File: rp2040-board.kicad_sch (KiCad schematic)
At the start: 100 parts, among them J1 24V IN, J10 E0-RUNOUT, J11 FAN1, J12 FAN2, J13 FAN3, J14 HB, J15 E0, J16 TH-E0, J2 USB4105-GF-A, J3 PGA2040, J4 3_GPIO, J5 PROBE, J6 X-ENDSTOP, J7 TH-HB, J8 Y-ENDSTOP, J9 Z-ENDSTOP, Q1 AO3400C, Q2 AO3400C, Q3 AO3400C, SW1 SW_MEC_5E, U1 LD1086DT33TR, U2 TPS5450DDAR, U3 74HCT365D,653, U4 FDS8896, U5 FDS8896

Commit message: almost done with layout...
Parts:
- removed D10, D11, D3, D7, D8, D9: Red LED, Diode_SMD:D_1210_3225Metric_Pad1.42x2.65mm_HandSolder, symbol Device:LED
- removed R3: 1K, Resistor_SMD:R_1206_3216Metric_Pad1.30x1.75mm_HandSolder, symbol Device:R_Small
- removed R35, R36, R37, R38, R39: 10K, Resistor_SMD:R_1206_3216Metric_Pad1.30x1.75mm_HandSolder, symbol Device:R_Small
- removed U1: LD1086DT33TR, LD1086DT33TR:VREG_L78M08CDT-TR, symbol LD1086DT33TR:LD1086DT33TR
- added U1: AMS1117-3.3, SOT229P700X180-4N, symbol AMS1117-3.3:AMS1117-3.3
- C1, C10, C2, C3: footprint Capacitor_SMD:C_1206_3216Metric_Pad1.33x1.80mm_HandSolder -> Capacitor_SMD:C_0805_2012Metric_Pad1.18x1.45mm_HandSolder
- C12, C13, C14, C15, C16, C17, C18, C4, C5, C8, C9: footprint Capacitor_SMD:C_1206_3216Metric_Pad1.33x1.80mm_HandSolder -> Capacitor_SMD:C_0805_2012Metric_Pad1.18x1.45mm_HandSolder; MANUFACTURER Murata -> Samsung Electro Mechanics
- C6: renamed from C7; footprint Capacitor_SMD:C_1210_3225Metric_Pad1.33x2.70mm_HandSolder -> Capacitor_SMD:C_0805_2012Metric_Pad1.18x1.45mm_HandSolder; MANUFACTURER Taiyo Yuden -> Murata
- C7: renamed from C6; footprint Capacitor_SMD:C_1206_3216Metric_Pad1.33x1.80mm_HandSolder -> Capacitor_SMD:C_0805_2012Metric_Pad1.18x1.45mm_HandSolder; MANUFACTURER Murata -> Samsung Electro Mechanics
- D1: footprint Diode_SMD:D_SMC_Handsoldering -> Diode_SMD:D_SMA_Handsoldering; MANUFACTURER onsemi -> MDD
- D2: footprint Diode_SMD:D_SMB-SMC_Universal_Handsoldering -> Diode_SMD:D_SMB_Handsoldering
- D3: renamed from D4; footprint Diode_SMD:D_SMC_Handsoldering -> Diode_SMD:D_SMA_Handsoldering
- F2: footprint 01000063Z:01000063Z -> 01000063Z; symbol Device:Fuse -> 01000063Z:01000063Z
- R1: footprint Resistor_SMD:R_1206_3216Metric_Pad1.30x1.75mm_HandSolder -> Resistor_SMD:R_0805_2012Metric_Pad1.20x1.40mm_HandSolder; MANUFACTURER Panasonic -> YAGEO
- R10: renamed from R11; footprint Resistor_SMD:R_1206_3216Metric_Pad1.30x1.75mm_HandSolder -> Resistor_SMD:R_0805_2012Metric_Pad1.20x1.40mm_HandSolder; MANUFACTURER Vishay Intertech -> YAGEO
- R11: renamed from R12; footprint Resistor_SMD:R_1206_3216Metric_Pad1.30x1.75mm_HandSolder -> Resistor_SMD:R_0805_2012Metric_Pad1.20x1.40mm_HandSolder; MANUFACTURER Vishay Intertech -> YAGEO
- R12: renamed from R13; footprint Resistor_SMD:R_1210_3225Metric_Pad1.30x2.65mm_HandSolder -> Resistor_SMD:R_0805_2012Metric_Pad1.20x1.40mm_HandSolder
- R13: renamed from R14; footprint Resistor_SMD:R_1210_3225Metric_Pad1.30x2.65mm_HandSolder -> Resistor_SMD:R_0805_2012Metric_Pad1.20x1.40mm_HandSolder
- R14: renamed from R15; footprint Resistor_SMD:R_1206_3216Metric_Pad1.30x1.75mm_HandSolder -> Resistor_SMD:R_0805_2012Metric_Pad1.20x1.40mm_HandSolder; MANUFACTURER Vishay Intertech -> YAGEO
- R15: renamed from R16; footprint Resistor_SMD:R_1206_3216Metric_Pad1.30x1.75mm_HandSolder -> Resistor_SMD:R_0805_2012Metric_Pad1.20x1.40mm_HandSolder; MANUFACTURER Vishay Intertech -> YAGEO
- R16: renamed from R17; footprint Resistor_SMD:R_1206_3216Metric_Pad1.30x1.75mm_HandSolder -> Resistor_SMD:R_0805_2012Metric_Pad1.20x1.40mm_HandSolder
- R17: renamed from R18; footprint Resistor_SMD:R_1206_3216Metric_Pad1.30x1.75mm_HandSolder -> Resistor_SMD:R_0805_2012Metric_Pad1.20x1.40mm_HandSolder; MANUFACTURER Panasonic -> YAGEO
- R18: renamed from R19; footprint Resistor_SMD:R_1206_3216Metric_Pad1.30x1.75mm_HandSolder -> Resistor_SMD:R_0805_2012Metric_Pad1.20x1.40mm_HandSolder
- R19: renamed from R20; footprint Resistor_SMD:R_1206_3216Metric_Pad1.30x1.75mm_HandSolder -> Resistor_SMD:R_0805_2012Metric_Pad1.20x1.40mm_HandSolder; MANUFACTURER Panasonic -> YAGEO
- R2: footprint Resistor_SMD:R_1206_3216Metric_Pad1.30x1.75mm_HandSolder -> Resistor_SMD:R_0805_2012Metric_Pad1.20x1.40mm_HandSolder; MANUFACTURER Vishay Intertech -> YAGEO
- R20: renamed from R21; footprint Resistor_SMD:R_1206_3216Metric_Pad1.30x1.75mm_HandSolder -> Resistor_SMD:R_0805_2012Metric_Pad1.20x1.40mm_HandSolder; MANUFACTURER Vishay Intertech -> YAGEO
- R21: renamed from R22; footprint Resistor_SMD:R_1206_3216Metric_Pad1.30x1.75mm_HandSolder -> Resistor_SMD:R_0805_2012Metric_Pad1.20x1.40mm_HandSolder; MANUFACTURER Vishay Intertech -> YAGEO
- R22: renamed from R23; footprint Resistor_SMD:R_1206_3216Metric_Pad1.30x1.75mm_HandSolder -> Resistor_SMD:R_0805_2012Metric_Pad1.20x1.40mm_HandSolder; MANUFACTURER Vishay Intertech -> YAGEO
- R23: renamed from R24; footprint Resistor_SMD:R_1206_3216Metric_Pad1.30x1.75mm_HandSolder -> Resistor_SMD:R_0805_2012Metric_Pad1.20x1.40mm_HandSolder; MANUFACTURER Vishay Intertech -> YAGEO
- R24: renamed from R25; footprint Resistor_SMD:R_1206_3216Metric_Pad1.30x1.75mm_HandSolder -> Resistor_SMD:R_0805_2012Metric_Pad1.20x1.40mm_HandSolder; MANUFACTURER Vishay Intertech -> YAGEO
- R25: renamed from R26; footprint Resistor_SMD:R_1210_3225Metric_Pad1.30x2.65mm_HandSolder -> Resistor_SMD:R_0805_2012Metric_Pad1.20x1.40mm_HandSolder
- R26: renamed from R27; footprint Resistor_SMD:R_1206_3216Metric_Pad1.30x1.75mm_HandSolder -> Resistor_SMD:R_0805_2012Metric_Pad1.20x1.40mm_HandSolder
- R27: renamed from R28; footprint Resistor_SMD:R_1206_3216Metric_Pad1.30x1.75mm_HandSolder -> Resistor_SMD:R_0805_2012Metric_Pad1.20x1.40mm_HandSolder; MANUFACTURER Panasonic -> YAGEO
- R28: renamed from R29; footprint Resistor_SMD:R_1206_3216Metric_Pad1.30x1.75mm_HandSolder -> Resistor_SMD:R_0805_2012Metric_Pad1.20x1.40mm_HandSolder
- R29: renamed from R30; footprint Resistor_SMD:R_1206_3216Metric_Pad1.30x1.75mm_HandSolder -> Resistor_SMD:R_0805_2012Metric_Pad1.20x1.40mm_HandSolder; MANUFACTURER Panasonic -> YAGEO
- R3: renamed from R4; footprint Resistor_SMD:R_1206_3216Metric_Pad1.30x1.75mm_HandSolder -> Resistor_SMD:R_0805_2012Metric_Pad1.20x1.40mm_HandSolder; MANUFACTURER Vishay Intertech -> YAGEO
- R30: renamed from R31; footprint Resistor_SMD:R_1206_3216Metric_Pad1.30x1.75mm_HandSolder -> Resistor_SMD:R_0805_2012Metric_Pad1.20x1.40mm_HandSolder
- R31: renamed from R32; footprint Resistor_SMD:R_1206_3216Metric_Pad1.30x1.75mm_HandSolder -> Resistor_SMD:R_0805_2012Metric_Pad1.20x1.40mm_HandSolder; MANUFACTURER Panasonic -> YAGEO
- R32: renamed from R33; footprint Resistor_SMD:R_1210_3225Metric_Pad1.30x2.65mm_HandSolder -> Resistor_SMD:R_0805_2012Metric_Pad1.20x1.40mm_HandSolder
- R33: renamed from R34; footprint Resistor_SMD:R_1206_3216Metric_Pad1.30x1.75mm_HandSolder -> Resistor_SMD:R_0805_2012Metric_Pad1.20x1.40mm_HandSolder; MANUFACTURER Vishay Intertech -> YAGEO
- R4: renamed from R5; footprint Resistor_SMD:R_1206_3216Metric_Pad1.30x1.75mm_HandSolder -> Resistor_SMD:R_0805_2012Metric_Pad1.20x1.40mm_HandSolder; MANUFACTURER Vishay Intertech -> YAGEO
- R5: renamed from R6; footprint Resistor_SMD:R_1210_3225Metric_Pad1.30x2.65mm_HandSolder -> Resistor_SMD:R_0805_2012Metric_Pad1.20x1.40mm_HandSolder
- R6: renamed from R7; footprint Resistor_SMD:R_1206_3216Metric_Pad1.30x1.75mm_HandSolder -> Resistor_SMD:R_0805_2012Metric_Pad1.20x1.40mm_HandSolder; MANUFACTURER Vishay Intertech -> YAGEO
- R7: renamed from R8; footprint Resistor_SMD:R_1206_3216Metric_Pad1.30x1.75mm_HandSolder -> Resistor_SMD:R_0805_2012Metric_Pad1.20x1.40mm_HandSolder; MANUFACTURER Vishay Intertech -> YAGEO
- R8: renamed from R9; footprint Resistor_SMD:R_1206_3216Metric_Pad1.30x1.75mm_HandSolder -> Resistor_SMD:R_0805_2012Metric_Pad1.20x1.40mm_HandSolder; MANUFACTURER Vishay Intertech -> YAGEO
- R9: renamed from R10; footprint Resistor_SMD:R_1206_3216Metric_Pad1.30x1.75mm_HandSolder -> Resistor_SMD:R_0805_2012Metric_Pad1.20x1.40mm_HandSolder; MANUFACTURER Vishay Intertech -> YAGEO
- RN1, RN2, RN3, RN4: footprint Resistor_SMD:R_Array_Convex_4x1206 -> Resistor_SMD:R_Array_Convex_4x0603; MANUFACTURER Bourns -> CTS Electronic Components
- SW1: footprint Button_Switch_SMD:SW_Push_1P1T_NO_CK_KSC6xxJ -> 1825966-1:SW_1825966-1
- renumbered D5 to D4, D6 to D5
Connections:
- net +3.3V: now also U1.2 (VOUT)
- net +5V: now also C14.1, U3.16 (VCC)
- net GND: now also U1.1 (ADJ/GND)
- net VCC: now also F2.1
- net at J1.1 (Pin_1): now also F2.3, F2.4; no longer D2.1 (A)
- net at J1.2 (Pin_2): now also D2.1 (A); no longer F2.1
- net at F1.2: now also U1.3 (VIN)
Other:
- moved on the sheet: C1, C10, C11, C12, C15, C2, C3, C5, C6, C7, C8, D1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

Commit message: I am in immense pain
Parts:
- removed SW1: SW_MEC_5E, 1825966-1:SW_1825966-1, symbol Switch:SW_MEC_5E
- added JP1: RUN, Connector_PinHeader_2.54mm:PinHeader_1x02_P2.54mm_Vertical, symbol Jumper:Jumper_2_Open
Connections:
- net GND: now also JP1.1 (A)
- net HEATERS: no longer R26.2, R27.2, U3.3 (1Y)
- net VCC: now also F2.3, F2.4, J14.1 (Pin_1), J15.1 (Pin_1); no longer F2.1, F2.2, J14.2 (Pin_2), J15.2 (Pin_2)
- net at U4.5 (DRAIN-3), U4.6 (DRAIN-2), U4.7 (DRAIN-1)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: now also J14.2 (Pin_2); no longer J14.1 (Pin_1)
- net at U5.5 (DRAIN-3), U5.6 (DRAIN-2), U5.7 (DRAIN-1)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: now also J15.2 (Pin_2); no longer J15.1 (Pin_1)
- net at C5.2, J3.A4 (RUN), R2.2: now also JP1.2 (B)
- new net: R26.2, R27.2, U3.3 (1Y)
- new net: F2.1, F2.2, J1.1 (Pin_1)
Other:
- moved on the sheet: F2, J14, J15

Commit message: finished, for now, finally
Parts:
- removed J4: 3_GPIO, Connector_PinSocket_2.54mm:PinSocket_1x03_P2.54mm_Vertical, symbol Connector:Conn_01x03_Female
- added J22: Exp. Header 2, Connector_PinHeader_2.54mm:PinHeader_1x02_P2.54mm_Vertical, symbol Connector:Conn_01x02_Male
- added J23: Exp. Header 3, Connector_PinHeader_2.54mm:PinHeader_1x02_P2.54mm_Vertical, symbol Connector:Conn_01x02_Male
- added J4: Exp. Header 1, symbol Connector:Conn_01x02_Male
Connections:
- net +3.3V: now also J22.1 (Pin_1)
- net +5V: now also J23.1 (Pin_1)
- net E0DIR: now also J3.G4 (GPIO14); no longer J3.G3 (GPIO12), RN4.1 (R1.1)
- net E0EN: now also J3.G3 (GPIO12); no longer J3.G4 (GPIO14), RN4.3 (R3.1)
- net E0STP: no longer RN4.2 (R2.1)
- net GND: now also J23.2 (Pin_2)
- net XDIR: now also J3.C2 (GPIO2); no longer J3.B1 (GPIO0), RN1.1 (R1.1)
- net XEN: now also J3.B1 (GPIO0); no longer J3.C2 (GPIO2), RN1.3 (R3.1)
- net XSTP: no longer RN1.2 (R2.1)
- net YDIR: now also J3.E2 (GPIO6); no longer J3.D2 (GPIO4), RN2.1 (R1.1)
- net YEN: now also J3.D2 (GPIO4); no longer J3.E2 (GPIO6), RN2.3 (R3.1)
- net YSTP: no longer RN2.2 (R2.1)
- net ZDIR: now also J3.H2 (GPIO10); no longer J3.F2 (GPIO8), RN3.1 (R1.1)
- net ZEN: now also J3.F2 (GPIO8); no longer J3.H2 (GPIO10), RN3.3 (R3.1)
- net ZSTP: no longer RN3.2 (R2.1)
- net GPIO22: now reaches J3.F7 (GPIO22)
- net GPIO22: now also J22.2 (Pin_2)
- net GPIO21: now reaches J3.F8 (GPIO21)
- net GPIO21: now also J4.2 (Pin_2)
- net GPIO20: now reaches J3.G8 (GPIO20)
- net GPIO20: now also J4.1 (Pin_1)
- new net E0DIRR: RN4.1 (R1.1)
- new net E0ENR: RN4.3 (R3.1)
- new net E0STPR: RN4.2 (R2.1)
- new net XDIRR: RN1.1 (R1.1)
- new net XENR: RN1.3 (R3.1)
- new net XSTPR: RN1.2 (R2.1)
- new net YDIRR: RN2.1 (R1.1)
- new net YENR: RN2.3 (R3.1)
- new net YSTPR: RN2.2 (R2.1)
- new net ZDIRR: RN3.1 (R1.1)
- new net ZENR: RN3.3 (R3.1)
- new net ZSTPR: RN3.2 (R2.1)
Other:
- moved on the sheet: RN1, RN2, RN3, RN4

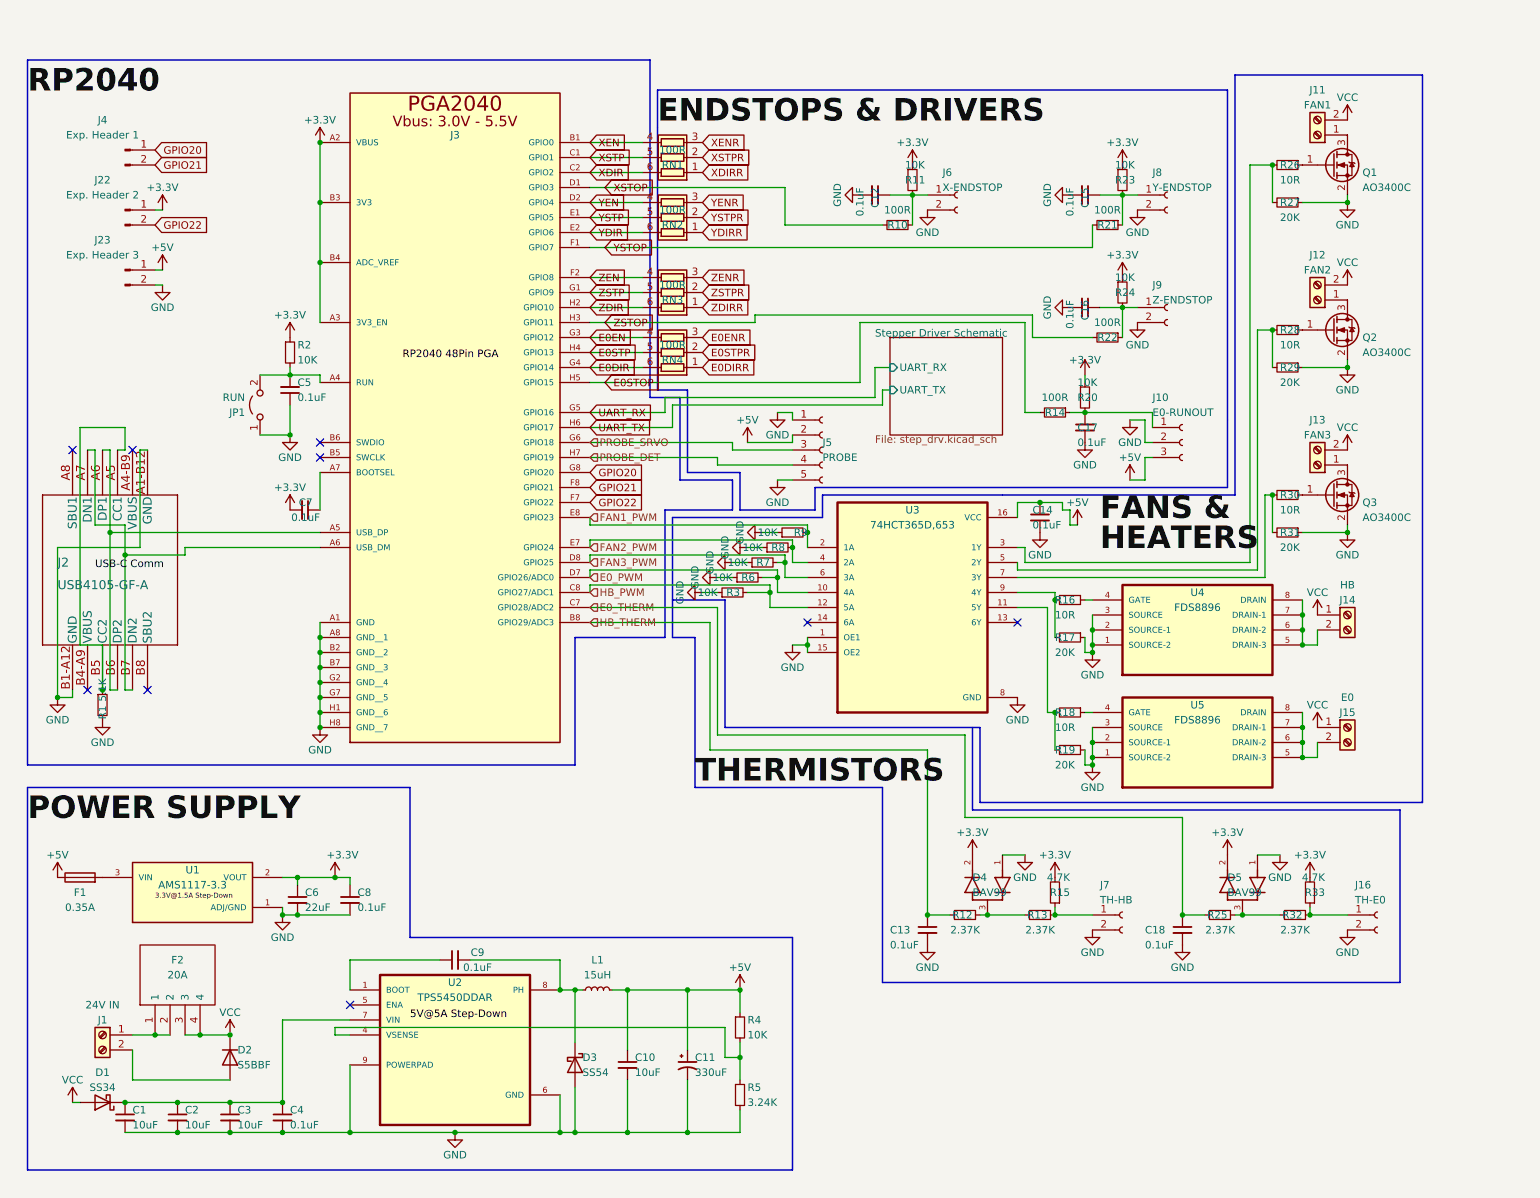
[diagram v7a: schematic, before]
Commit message: Rev 1.1 - PT1000 + ADC/I2C GPIO
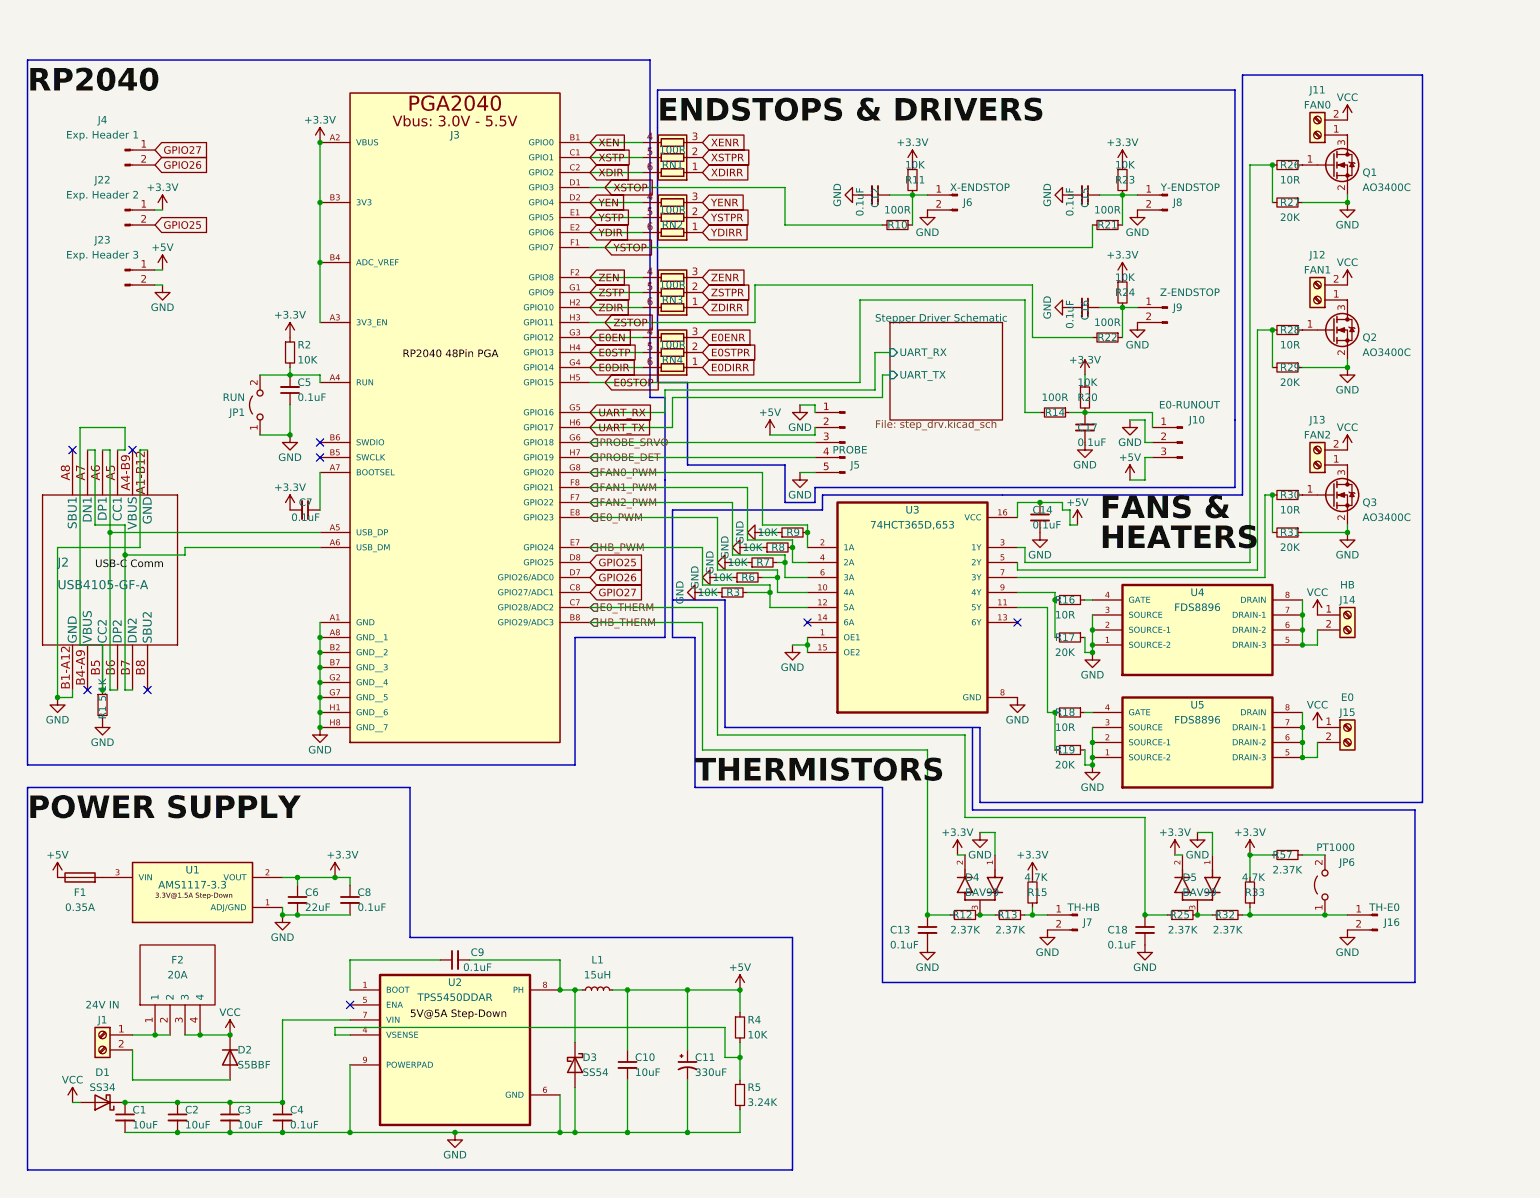
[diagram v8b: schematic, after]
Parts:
- added JP6: PT1000, Connector_PinHeader_2.54mm:PinHeader_1x02_P2.54mm_Vertical, symbol Jumper:Jumper_2_Open
- added R57: 2.37K, Resistor_SMD:R_0805_2012Metric_Pad1.20x1.40mm_HandSolder, symbol Device:R_Small
- J10: symbol Connector:Conn_01x03_Female -> Connector:Conn_01x03_Male
- J11: value FAN1 -> FAN0
- J12: value FAN2 -> FAN1
- J13: value FAN3 -> FAN2
- J16, J6, J7, J8, J9: symbol Connector:Conn_01x02_Female -> Connector:Conn_01x02_Male
- J4: footprint (none) -> Connector_PinHeader_2.54mm:PinHeader_1x02_P2.54mm_Vertical
- J5: symbol Connector:Conn_01x05_Female -> Connector:Conn_01x05_Male
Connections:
- net +3.3V: now also R57.2
- net E0_PWM: now also J3.E8 (GPIO23); no longer J3.D7 (GPIO26/ADC0)
- net FAN1_PWM: now also J3.F8 (GPIO21), R8.2, U3.4 (2A); no longer J3.E8 (GPIO23), R9.2, U3.2 (1A)
- net FAN2_PWM: now also J3.F7 (GPIO22), R7.2, U3.6 (3A); no longer J3.E7 (GPIO24), R8.2, U3.4 (2A)
- net HB_PWM: now also J3.E7 (GPIO24); no longer J3.C8 (GPIO27/ADC1)
- net at J16.1 (Pin_1), R32.2, R33.1: now also JP6.1 (A)
- removed net FAN3_PWM: J3.D8 (GPIO25), R7.2, U3.6 (3A)
- net GPIO20 renamed FAN0_PWM
- net FAN0_PWM: now also R9.2, U3.2 (1A); no longer J4.1 (Pin_1)
- net GPIO21 renamed GPIO26
- net GPIO26: now also J3.D7 (GPIO26/ADC0); no longer J3.F8 (GPIO21)
- net GPIO22 renamed GPIO25
- net GPIO25: now also J3.D8 (GPIO25); no longer J3.F7 (GPIO22)
- new net: JP6.2 (B), R57.1
- new net GPIO27: J3.C8 (GPIO27/ADC1), J4.1 (Pin_1)
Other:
- moved on the sheet: C18, D4, D5, R13, R15, R25, R32, R33
